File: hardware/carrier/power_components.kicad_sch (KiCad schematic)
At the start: 38 parts, among them J6 USB4235, J7 BATTERY, Q4 AO3401A, SW2 JS102011SAQN, U5 BQ25185DLHR, U6 MAX17048G+T10, U7 TPS62840DLCR

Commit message: Replace JP1 with 0402 0R link, shrink SW1/SW2 to KMR2 and MSK12C02
JP1 (solder jumper) becomes R39, a fitted 0402 0R on the auto-boot line:
pull it to disable auto boot. SW1 is now a C&K KMR221GLFS (4.2 x 2.8 x
1.3 mm, C72443) and SW2 a Shou Han MSK12C02 top-knob slide switch
(C431540). Footprints swapped in the PCB with nets preserved (SW1 pads
now carry FL_BTN/GND). Adds the JLCPCB design rules file.

Co-Authored-By: Claude Fable 5.1 <noreply@anthropic.com>
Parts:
- SW2: value JS102011SAQN -> MSK12C02; footprint Button_Switch_SMD:SW_SPDT_CK_JS102011SAQN -> Button_Switch_SMD:SW_SPDT_Shouhan_MSK12C02; LCSC C221660 -> C431540; MPN JS102011SAQN -> MSK12C02
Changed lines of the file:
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@@
 			)
 		)
-		(property "Value" "JS102011SAQN"
+		(property "Value" "MSK12C02"
 			(at 59.69 112.776 90)
 			(show_name no)
@@
 			)
 		)
-		(property "Footprint" "Button_Switch_SMD:SW_SPDT_CK_JS102011SAQN"
+		(property "Footprint" "Button_Switch_SMD:SW_SPDT_Shouhan_MSK12C02"
 			(at 64.77 127 0)
 			(hide yes)
@@
 			)
 		)
-		(property "MPN" "JS102011SAQN"
+		(property "MPN" "MSK12C02"
 			(at 77.47 120.65 0)
 			(hide yes)
@@
 			)
 		)
-		(property "LCSC" "C221660"
+		(property "LCSC" "C431540"
 			(at 80.01 120.65 0)
 			(hide yes)

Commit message: Carrier schematics: owner's updates to core and power sheets
Owner edits made in KiCad alongside the v0.2c layout work (library symbol
and sheet changes in core_components and power_components).

Co-Authored-By: Claude Fable 5.1 <noreply@anthropic.com>
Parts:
- removed TP6: GND, TestPoint:TestPoint_Pad_1.0x1.0mm, symbol Connector:TestPoint
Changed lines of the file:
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@@
 	(wire
 		(pts
-			(xy 196.85 114.3) (xy 196.85 111.76)
-		)
-		(stroke
-			(width 0)
-			(type default)
-		)
-	)
-	(wire
-		(pts
 			(xy 40.64 121.92) (xy 40.64 124.46)
 		)
@@
 	)
 	(symbol
-		(lib_id "Connector:TestPoint")
-		(at 196.85 114.3 0)
-		(mirror x)
-		(unit 1)
-		(body_style 1)
-		(exclude_from_sim no)
-		(in_bom yes)
-		(on_board yes)
-		(in_pos_files yes)
-		(dnp no)
-		(property "Reference" "TP6"
-			(at 198.12 115.57 0)
-			(show_name no)
-			(do_not_autoplace no)
-			(effects
-				(font
-					(size 1.27 1.27)
-				)
-				(justify left)
-			)
-		)
-		(property "Value" "GND"
-			(at 198.12 113.03 0)
-			(show_name no)
-			(do_not_autoplace no)
-			(effects
-				(font
-					(size 1.27 1.27)
-				)
-				(justify left)
-			)
-		)
-		(property "Footprint" "TestPoint:TestPoint_Pad_1.0x1.0mm"
-			(at 198.12 110.49 0)
-			(hide yes)
-			(show_name no)
-			(do_not_autoplace no)
-			(effects
-				(font
-					(size 1.27 1.27)
-				)
-				(justify left)
-			)
-		)
-		(property "Datasheet" "~"
-			(at 198.12 107.95 0)
-			(hide yes)
-			(show_name no)
-			(do_not_autoplace no)
-			(effects
-				(font
-					(size 1.27 1.27)
-				)
-				(justify left)
-			)
-		)
-		(property "Description" "test point"
-			(at 198.12 105.41 0)
-			(hide yes)
-			(show_name no)
-			(do_not_autoplace no)
-			(effects
-				(font
-					(size 1.27 1.27)
-				)
-				(justify left)
-			)
-		)
-		(property "MPN" ""
-			(at 196.85 99.06 0)
-			(hide yes)
-			(show_name no)
-			(do_not_autoplace no)
-			(effects
-				(font
-					(size 1.27 1.27)
-				)
-			)
-		)
-		(property "LCSC" ""
-			(at 196.85 96.52 0)
-			(hide yes)
-			(show_name no)
-			(do_not_autoplace no)
-			(effects
-				(font
-					(size 1.27 1.27)
-				)
-			)
-		)
-		(property "DNP" ""
-			(at 196.85 93.98 0)
-			(hide yes)
-			(show_name no)
-			(do_not_autoplace no)
-			(effects
-				(font
-					(size 1.27 1.27)
-				)
-			)
-		)
-		(property "Note" "test pad"
-			(at 196.85 91.44 0)
-			(hide yes)
-			(show_name no)
-			(do_not_autoplace no)
-			(effects
-				(font
-					(size 1.27 1.27)
-				)
-			)
-		)
-		(pin "1"
-		)
-		(instances
-			(project "pager-carrier"
-				(path "/ab8ee99e-0f89-4d3d-ba18-cf2cd7eb7e8f"
-					(reference "TP6")
-					(unit 1)
-				)
-			)
-		)
-	)
-	(symbol
 		(lib_id "Device:R")
 		(at 83.82 120.65 0)
@@
 	)
 	(symbol
-		(lib_id "power:GND")
-		(at 196.85 111.76 0)
-		(mirror x)
-		(unit 1)
-		(body_style 1)
-		(exclude_from_sim no)
-		(in_bom no)
-		(on_board no)
-		(in_pos_files yes)
-		(dnp no)
-		(property "Reference" "#PWR026"
-			(at 196.85 111.76 0)
-			(hide yes)
-			(show_name no)
-			(do_not_autoplace no)
-			(effects
-				(font
-					(size 1.27 1.27)
-				)
-				(justify left)
-			)
-		)
-		(property "Value" "GND"
-			(at 196.85 107.95 0)
-			(show_name no)
-			(do_not_autoplace no)
-			(effects
-				(font
-					(size 1.27 1.27)
-				)
-				(justify left)
-			)
-		)
-		(property "Footprint" ""
-			(at 196.85 111.76 0)
-			(hide yes)
-			(show_name no)
-			(do_not_autoplace no)
-			(effects
-				(font
-					(size 1.27 1.27)
-				)
-				(justify left)
-			)
-		)
-		(property "Datasheet" "~"
-			(at 196.85 111.76 0)
-			(hide yes)
-			(show_name no)
-			(do_not_autoplace no)
-			(effects
-				(font
-					(size 1.27 1.27)
-				)
-				(justify left)
-			)
-		)
-		(property "Description" "Power symbol"
-			(at 196.85 111.76 0)
-			(hide yes)
-			(show_name no)
-			(do_not_autoplace no)
-			(effects
-				(font
-					(size 1.27 1.27)
-				)
-				(justify left)
-			)
-		)
-		(pin "1"
-		)
-		(instances
-			(project "pager-carrier"
-				(path "/ab8ee99e-0f89-4d3d-ba18-cf2cd7eb7e8f"
-					(reference "#PWR026")
-					(unit 1)
-				)
-			)
-		)
-	)
-	(symbol
 		(lib_id "Device:R")
 		(at 63.5 49.53 0)
@@
 	)
 	(group ""
-		(members "3a2ca3d9-ff4b-40e9-898d-326beab9ef7e" "4561f15c-bc9d-4ce2-a3a7-df164aab50f6"
-			"55a85c6e-d843-4d73-9166-1661dcaa8083" "679bd483-ad52-4982-b03d-4d408d27165d"
-			"68f1d099-16ff-4d0c-8671-156cbcd2ad65" "8c7a8631-58d4-4879-ab4e-11996f1f77a4"
-			"a6f04a96-1df1-44e1-bccf-2742e6c9256f" "b04b7a03-8063-4344-bb55-f37c45820f5b"
-			"b49c684b-b4e7-4219-a8ee-95147af5ea61" "d3f97163-9862-4aa1-b408-97be8e86bae2"
-			"d6c92a88-2333-4d91-93c8-9cf459e2c3e4" "dd6bc7c2-3c29-483d-bcd9-02e2d4f04b95"
-			"df7da108-8619-4416-8bf7-b7fa0bc4cb65" "e3acfa41-4661-4121-8443-7c2441d850d3"
-			"e65bd0ea-dbcb-4ddc-bd69-6eb3a8a7c2d0" "e70cec4b-c0fd-4931-8b4b-80ce8a71773f"
-			"ed54c504-aa86-4a64-ada2-fe4bb24159cb" "fb0d3f25-ade3-4b2a-a98e-b3a94d306b2d"
+		(members "3a2ca3d9-ff4b-40e9-898d-326beab9ef7e" "55a85c6e-d843-4d73-9166-1661dcaa8083"
+			"679bd483-ad52-4982-b03d-4d408d27165d" "68f1d099-16ff-4d0c-8671-156cbcd2ad65"
+			"8c7a8631-58d4-4879-ab4e-11996f1f77a4" "a6f04a96-1df1-44e1-bccf-2742e6c9256f"
+			"b49c684b-b4e7-4219-a8ee-95147af5ea61" "d6c92a88-2333-4d91-93c8-9cf459e2c3e4"
+			"dd6bc7c2-3c29-483d-bcd9-02e2d4f04b95" "df7da108-8619-4416-8bf7-b7fa0bc4cb65"
+			"e3acfa41-4661-4121-8443-7c2441d850d3" "e65bd0ea-dbcb-4ddc-bd69-6eb3a8a7c2d0"
+			"e70cec4b-c0fd-4931-8b4b-80ce8a71773f" "ed54c504-aa86-4a64-ada2-fe4bb24159cb"
+			"fb0d3f25-ade3-4b2a-a98e-b3a94d306b2d"
 		)
 	)

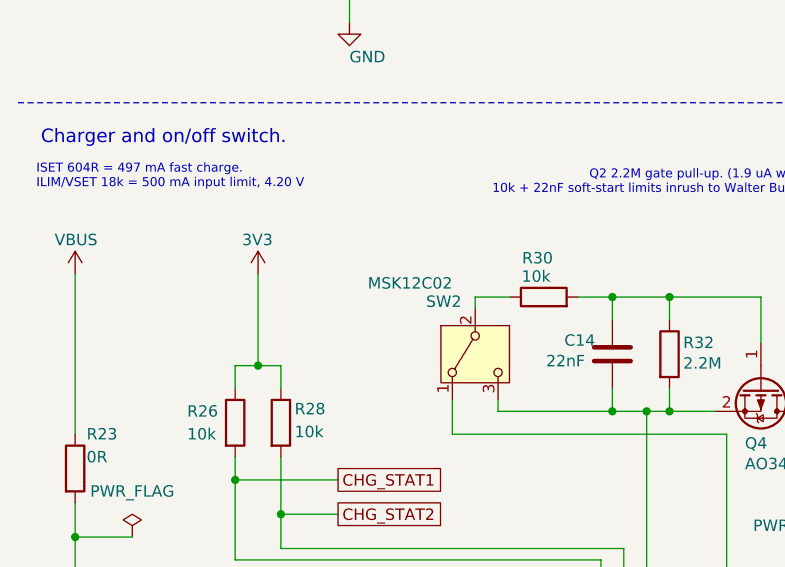
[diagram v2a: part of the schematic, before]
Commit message: Carrier v0.2c WIP: cassette screw holes, top-actuated SW2, wider board, panel schematic fixes
Work in progress for the 3D-printed display cassette; routing is DRC-clean
(0 errors) with 14 signal links and 3 ground islands left for hand finishing
(list in HANDOFF-v0.2.md).

Carrier:
- H1-H3 M2 cassette screw holes (2.2 mm NPTH, 4.5 mm copper-free annulus on
  both layers via footprint rule areas + per-hole DRC rules) at (77.4, 60.9),
  (111.2, 59.95), (111.2, 105.85); schematic symbols in the core sheet.
- SW2 power switch -> C&K JS102011SAQN top-actuated SPDT (LCSC C221660),
  travel along X; top strip is now J6, SW1, SW2 (x 80.0..108.5).
- Board widened to x 120.5 so the right-side holes fit beside the header
  column (J2 keyboard header stays topmost, cable into the plate channel).
- F.Fab note to trim the Walter header pins flush; stale KBD label moved.
- 3D models added: JS102011SAQN, MAX17048 (U6), JST PH S2B-PH-SM4-TB (J7);
  STEP export in out/ for the Fusion assembly.
- Owner's manual schematic edits (test points) included.

Panel:
- Owner's rearranged panel_main.kicad_sch with the EPD_GDR wire gap closed
  (J1 pin 2 back on the boost gate net); both front-light FPC connectors kept.

Co-Authored-By: Claude Fable 5.1 <noreply@anthropic.com>
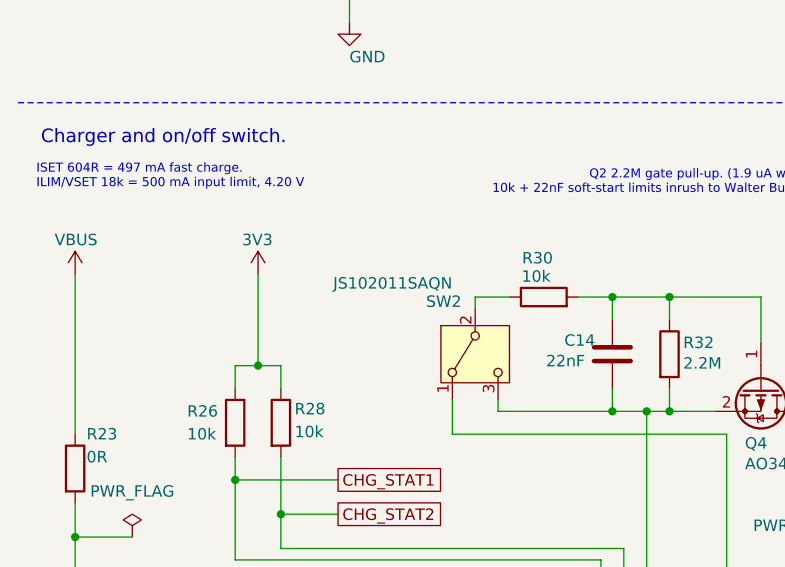
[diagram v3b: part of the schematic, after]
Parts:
- SW2: value MSK12C02 -> JS102011SAQN; footprint Button_Switch_SMD:SW_SPDT_Shouhan_MSK12C02 -> Button_Switch_SMD:SW_SPDT_CK_JS102011SAQN; LCSC C431540 -> C221660; MPN MSK12C02 -> JS102011SAQN
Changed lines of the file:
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@@
 			)
 		)
-		(property "Value" "MSK12C02"
+		(property "Value" "JS102011SAQN"
 			(at 59.69 112.776 90)
 			(show_name no)
@@
 			)
 		)
-		(property "Footprint" "Button_Switch_SMD:SW_SPDT_Shouhan_MSK12C02"
+		(property "Footprint" "Button_Switch_SMD:SW_SPDT_CK_JS102011SAQN"
 			(at 64.77 127 0)
 			(hide yes)
@@
 			)
 		)
-		(property "Datasheet" "~"
+		(property "Datasheet" "https://www.ckswitches.com/media/1422/js.pdf"
 			(at 67.31 127 0)
 			(hide yes)
@@
 			)
 		)
-		(property "Description" "Switch, single pole double throw"
+		(property "Description" "SPDT slide switch, top actuated, SMD gull wing, C&K JS series (3.5 mm overall incl. knob)"
 			(at 69.85 127 0)
 			(hide yes)
@@
 			)
 		)
-		(property "MPN" "MSK12C02"
+		(property "MPN" "JS102011SAQN"
 			(at 77.47 120.65 0)
 			(hide yes)
@@
 			)
 		)
-		(property "LCSC" "C431540"
+		(property "LCSC" "C221660"
 			(at 80.01 120.65 0)
 			(hide yes)

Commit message: Carrier: battery connector J7 -> JST SH SM02B-SRSS-TB (LCSC C160402)
Replaces the 5.5 mm JST PH S2B-PH-SM4-TB, which sat above the display glass back.
SH side-entry is 2.9 mm tall and matches J3/J4/J5. Schematic fields, board footprint
(KiCad library model), VBAT stub re-hooked, pours refilled. ERC 0, DRC 0 errors,
9 unconnected (unchanged). STEP re-exported. Handoff notes the J2 MPN/footprint mismatch.

Co-Authored-By: Claude Fable 5.1 <noreply@anthropic.com>
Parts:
- J7: footprint Connector_JST:JST_PH_S2B-PH-SM4-TB_1x02-1MP_P2.00mm_Horizontal -> Connector_JST:JST_SH_SM02B-SRSS-TB_1x02-1MP_P1.00mm_Horizontal; LCSC C295747 -> C160402; MPN S2B-PH-SM4-TB -> SM02B-SRSS-TB
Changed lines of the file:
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@@
 			)
 		)
-		(property "Footprint" "Connector_JST:JST_PH_S2B-PH-SM4-TB_1x02-1MP_P2.00mm_Horizontal"
+		(property "Footprint" "Connector_JST:JST_SH_SM02B-SRSS-TB_1x02-1MP_P1.00mm_Horizontal"
 			(at 119.38 133.35 0)
 			(hide yes)
@@
 			)
 		)
-		(property "MPN" "S2B-PH-SM4-TB"
+		(property "MPN" "SM02B-SRSS-TB"
 			(at 130.81 129.54 0)
 			(hide yes)
@@
 			)
 		)
-		(property "LCSC" "C295747"
+		(property "LCSC" "C160402"
 			(at 133.35 129.54 0)
 			(hide yes)

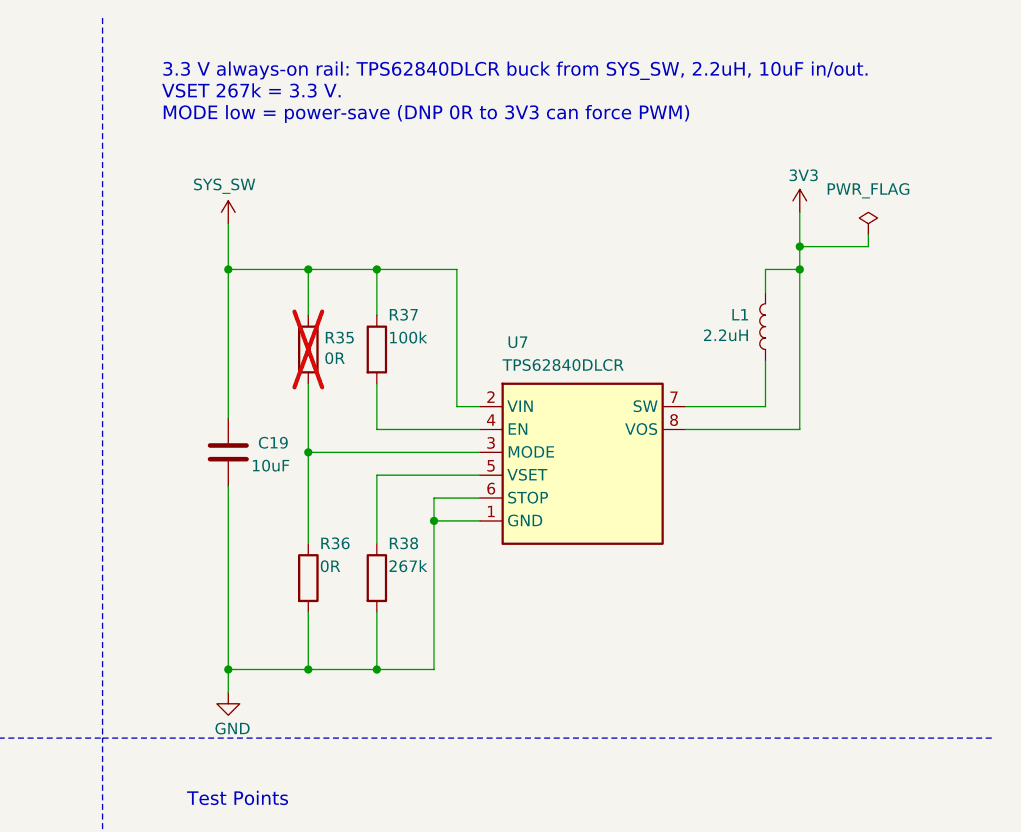
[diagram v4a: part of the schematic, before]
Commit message: Carrier: hand-layout in progress, USB circuit first (owner)
Autorouted tracks ripped up (1059 -> 448 segments, 149 -> 41 vias) for the
all-top-side hand layout. R35/R36 (U7 MODE 0R straps) removed from the schematic
and board. STEP re-exported.

Co-Authored-By: Claude Fable 5.1 <noreply@anthropic.com>
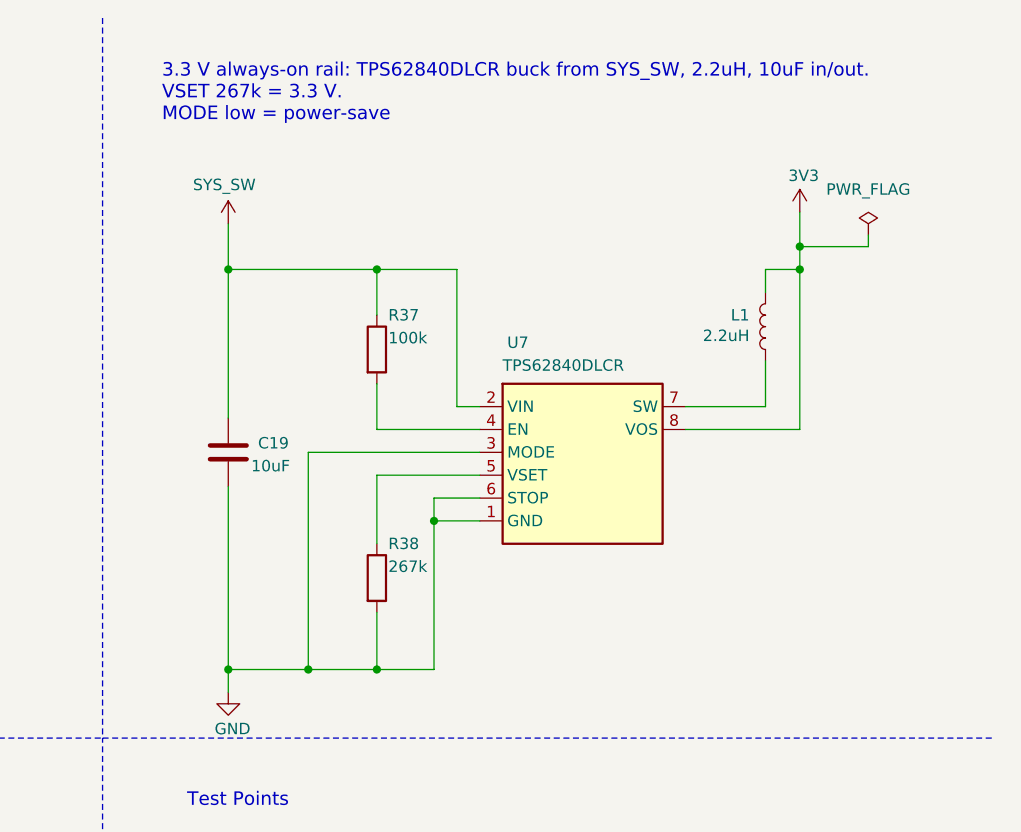
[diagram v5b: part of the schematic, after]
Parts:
- removed R35, R36: 0R, Resistor_SMD:R_0402_1005Metric, symbol Device:R
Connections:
- net GND: now also U7.3 (MODE)
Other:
- note added: "3.3 V always-on rail: TPS62840DLCR buck from SYS_SW, 2.2uH, 10uF in/out. VSET 267k = 3.3 V. MODE low = power-save"
- note removed: "3.3 V always-on rail: TPS62840DLCR buck from SYS_SW, 2.2uH, 10uF in/out. VSET 267k = 3.3 V. MODE low = power-save (DNP 0R to 3V3 can force PWM)"
